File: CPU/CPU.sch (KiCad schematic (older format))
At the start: 13 parts, among them J101 Conn_02x10_Odd_Even, J102 Conn_01x07_Female, Q101 IRLML0040TR, Q102 IRLML0040TR, SW101 SW_SPDT

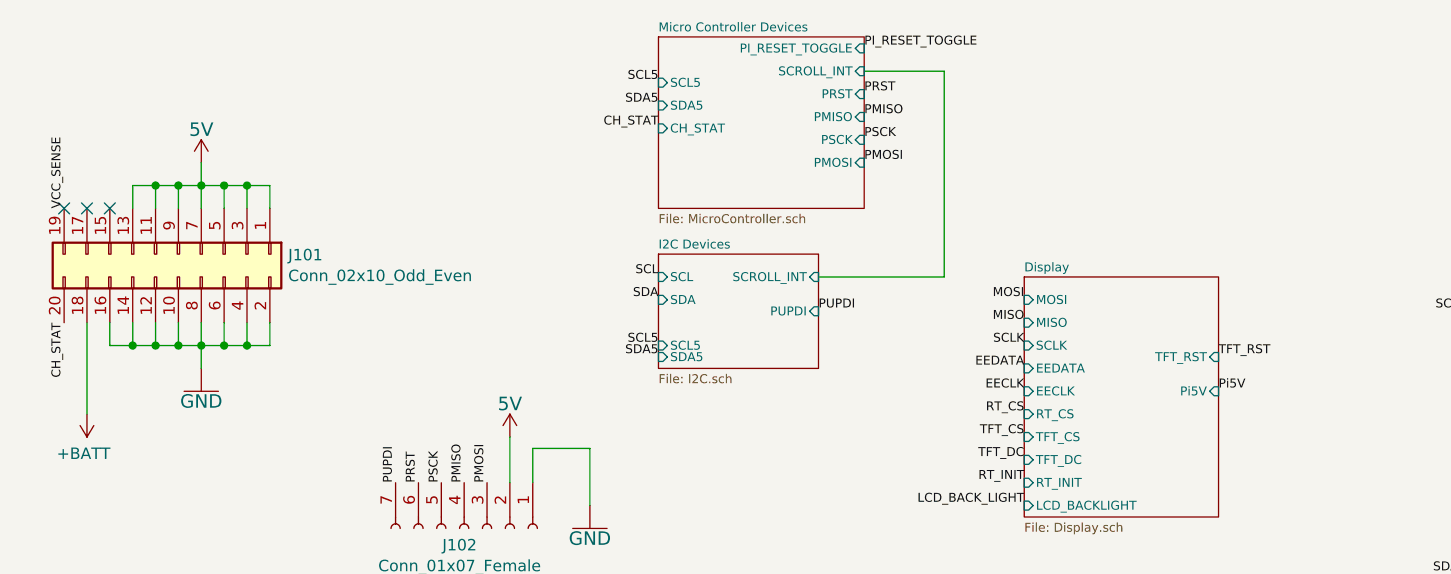
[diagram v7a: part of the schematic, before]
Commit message: Version 4 of the CPU board ordered with this commit.
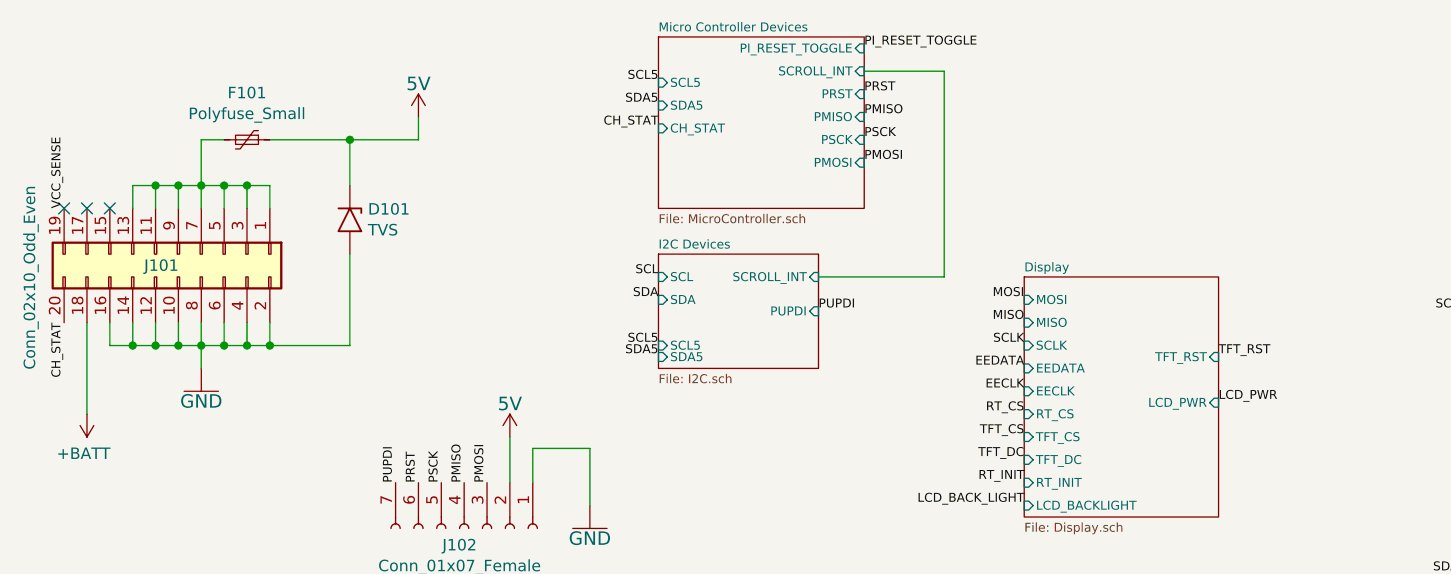
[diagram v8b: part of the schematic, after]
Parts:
- added D101: TVS, Diode_SMD:D_SMB-SMC_Universal_Handsoldering, symbol Diode:1N62xxA
- added F101: Polyfuse_Small, Fuse:Fuse_1210_3225Metric_Pad1.42x2.65mm_HandSolder, symbol Device:Polyfuse_Small
- J102: Customer Reference (none) -> CR101-V3
- R101, R102, R103, R104: LCSC Part Number C17414 -> C17520
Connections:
- net at J101.1 (Pin_1), J101.11 (Pin_11), J101.13 (Pin_13)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: now also F101.2
- net at J101.10 (Pin_10), J101.12 (Pin_12), J101.14 (Pin_14)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: now also D101.2 (A2)
- new net: D101.1 (A1), F101.1
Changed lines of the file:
@@
 U 1 1 5E842027
 P 1850 1700
-F 0 "J101" V 1854 2180 50  0000 L CNN
-F 1 "Conn_02x10_Odd_Even" V 1945 2180 50  0000 L CNN
+F 0 "J101" V 1900 1550 50  0000 L CNN
+F 1 "Conn_02x10_Odd_Even" H 1550 1050 50  0000 L CNN
 F 2 "Connector_PinHeader_2.00mm:PinHeader_2x10_P2.00mm_Vertical_SMD" H 1850 1700 50  0001 C CNN
 F 3 "~" H 1850 1700 50  0001 C CNN
@@
 Wire Wire Line
 	1750 1400 1850 1400
-Wire Wire Line
-	1950 1400 1950 1300
 $Comp
 L CPU-eagle-import:5V #SUPPLY0101
 U 1 1 5E870C32
-P 1950 1300
-F 0 "#SUPPLY0101" H 1950 1300 50  0001 C CNN
-F 1 "5V" H 1950 1410 59  0000 C BNN
-F 2 "" H 1950 1300 50  0001 C CNN
-F 3 "" H 1950 1300 50  0001 C CNN
-	1    1950 1300
+P 2900 1100
+F 0 "#SUPPLY0101" H 2900 1100 50  0001 C CNN
+F 1 "5V" H 2900 1210 59  0000 C BNN
+F 2 "" H 2900 1100 50  0001 C CNN
+F 3 "" H 2900 1100 50  0001 C CNN
+	1    2900 1100
 	1    0    0    -1
 $EndComp
@@
 F 2 "Resistor_SMD:R_0805_2012Metric_Pad1.15x1.40mm_HandSolder" H 7600 2800 50  0001 C CNN
 F 3 "" H 7600 2800 50  0001 C CNN
-F 4 " C17414" H 7600 2800 50  0001 C CNN "LCSC Part Number"
+F 4 "C17520" H 7600 2800 50  0001 C CNN "LCSC Part Number"
 F 5 "RC0805FR-0710KL" H 7600 2800 50  0001 C CNN "DigiKey"
 F 6 "CR101-V3" H 7600 2800 50  0001 C CNN "Customer Reference"
@@
 F 2 "Resistor_SMD:R_0805_2012Metric_Pad1.15x1.40mm_HandSolder" H 8100 2800 50  0001 C CNN
 F 3 "" H 8100 2800 50  0001 C CNN
-F 4 " C17414" H 8100 2800 50  0001 C CNN "LCSC Part Number"
+F 4 "C17520" H 8100 2800 50  0001 C CNN "LCSC Part Number"
 F 5 "RC0805FR-0710KL" H 8100 2800 50  0001 C CNN "DigiKey"
 F 6 "CR101-V3" H 8100 2800 50  0001 C CNN "Customer Reference"
@@
 F 2 "Resistor_SMD:R_0805_2012Metric_Pad1.15x1.40mm_HandSolder" H 7600 1650 50  0001 C CNN
 F 3 "" H 7600 1650 50  0001 C CNN
-F 4 " C17414" H 7600 1650 50  0001 C CNN "LCSC Part Number"
+F 4 "C17520" H 7600 1650 50  0001 C CNN "LCSC Part Number"
 F 5 "RC0805FR-0710KL" H 7600 1650 50  0001 C CNN "DigiKey"
 F 6 "CR101-V3" H 7600 1650 50  0001 C CNN "Customer Reference"
@@
 F 2 "Resistor_SMD:R_0805_2012Metric_Pad1.15x1.40mm_HandSolder" H 8100 1650 50  0001 C CNN
 F 3 "" H 8100 1650 50  0001 C CNN
-F 4 " C17414" H 8100 1650 50  0001 C CNN "LCSC Part Number"
+F 4 "C17520" H 8100 1650 50  0001 C CNN "LCSC Part Number"
 F 5 "RC0805FR-0710KL" H 8100 1650 50  0001 C CNN "DigiKey"
 F 6 "CR101-V3" H 8100 1650 50  0001 C CNN "Customer Reference"
@@
 F10 "RT_INIT" I L 5550 2700 39
 F11 "LCD_BACKLIGHT" I L 5550 2800 39
-F12 "Pi5V" I R 6400 2300 39
-F13 "TFT_RST" I R 6400 2150 39
+F12 "TFT_RST" I R 6400 2150 39
+F13 "LCD_PWR" I R 6400 2350 39
 $EndSheet
 Text Label 5550 2700 2    39   ~ 0
@@
 Wire Wire Line
 	4950 5400 5550 5400
-Text Label 6400 2300 0    39   ~ 0
-Pi5V
 $Comp
 L Connector:Conn_01x07_Female J102
@@
 F 3 "~" H 3100 2900 50  0001 C CNN
 F 4 "SM07B-SHLS-TF(LF)(SN)" V 3100 2900 50  0001 C CNN "DigiKey"
+F 5 "CR101-V3" H 3100 2900 50  0001 C CNN "Customer Reference"
 	1    3100 2900
 	0    1    1    0
@@
 Text Label 3050 5100 2    39   ~ 0
 SDA
+Text Label 6400 2350 0    39   ~ 0
+LCD_PWR
+$Comp
+L Device:Polyfuse_Small F101
+U 1 1 5F120D55
+P 2150 1200
+F 0 "F101" V 1945 1200 50  0000 C CNN
+F 1 "Polyfuse_Small" V 2036 1200 50  0000 C CNN
+F 2 "Fuse:Fuse_1210_3225Metric_Pad1.42x2.65mm_HandSolder" H 2200 1000 50  0001 L CNN
+F 3 "~" H 2150 1200 50  0001 C CNN
+F 4 "CR101-V3" H 2150 1200 50  0001 C CNN "Customer Reference"
+F 5 "PTSLR12066V110" H 2150 1200 50  0001 C CNN "DigiKey"
+	1    2150 1200
+	0    1    1    0
+$EndComp
+Wire Wire Line
+	1950 1200 2050 1200
+Wire Wire Line
+	1950 1200 1950 1400
+$Comp
+L Diode:1N62xxA D101
+U 1 1 5F1246DD
+P 2600 1550
+F 0 "D101" V 2554 1629 50  0000 L CNN
+F 1 "TVS" V 2645 1629 50  0000 L CNN
+F 2 "Diode_SMD:D_SMB-SMC_Universal_Handsoldering" H 2600 1350 50  0001 C CNN
+F 3 "https://www.vishay.com/docs/88301/15ke.pdf" H 2550 1550 50  0001 C CNN
+F 4 "CR101-V3" H 2600 1550 50  0001 C CNN "Customer Reference"
+F 5 "SMBJ5V0A" H 2600 1550 50  0001 C CNN "DigiKey"
+	1    2600 1550
+	0    1    1    0
+$EndComp
+Wire Wire Line
+	2250 1200 2600 1200
+Wire Wire Line
+	2600 1200 2600 1400
+Wire Wire Line
+	2600 1700 2600 2100
+Wire Wire Line
+	2600 2100 2250 2100
+Connection ~ 2250 2100
+Wire Wire Line
+	2600 1200 2900 1200
+Wire Wire Line
+	2900 1200 2900 1100
+Connection ~ 2600 1200
 $EndSCHEMATC
